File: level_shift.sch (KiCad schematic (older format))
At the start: 3 parts, among them Q1 BSS138

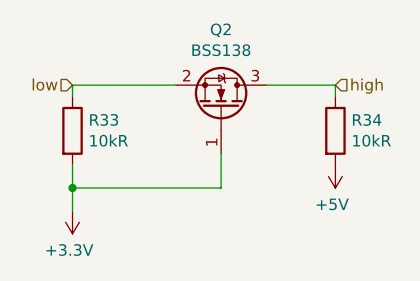
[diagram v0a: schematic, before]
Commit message: with cms resistors
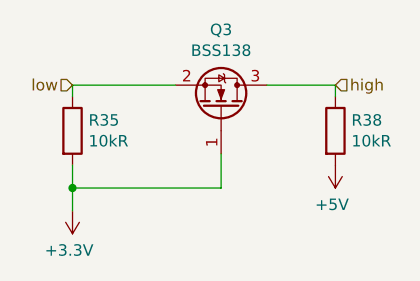
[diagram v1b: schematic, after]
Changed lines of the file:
@@
 AR Path="/619197DB/61901F6C" Ref="Q2"  Part="1"
 AR Path="/6191A86C/61901F6C" Ref="Q3"  Part="1"
-F 0 "Q2" V 4192 2200 50  0000 C CNN
+F 0 "Q3" V 4192 2200 50  0000 C CNN
 F 1 "BSS138" V 4101 2200 50  0000 C CNN
 F 2 "Package_TO_SOT_SMD:SOT-23" H 4050 2125 50  0001 L CIN
@@
 AR Path="/619197DB/61905F85" Ref="R33"  Part="1"
 AR Path="/6191A86C/61905F85" Ref="R35"  Part="1"
-F 0 "R33" H 3270 2346 50  0000 L CNN
+F 0 "R35" H 3270 2346 50  0000 L CNN
 F 1 "10kR" H 3270 2255 50  0000 L CNN
 F 2 "Resistor_SMD:R_0805_2012Metric_Pad1.20x1.40mm_HandSolder" V 3130 2300 50  0001 C CNN
@@
 AR Path="/619197DB/619062D3" Ref="R34"  Part="1"
 AR Path="/6191A86C/619062D3" Ref="R38"  Part="1"
-F 0 "R34" H 4420 2346 50  0000 L CNN
+F 0 "R38" H 4420 2346 50  0000 L CNN
 F 1 "10kR" H 4420 2255 50  0000 L CNN
 F 2 "Resistor_SMD:R_0805_2012Metric_Pad1.20x1.40mm_HandSolder" V 4280 2300 50  0001 C CNN
@@
 AR Path="/619197DB/619071C9" Ref="#PWR0105"  Part="1"
 AR Path="/6191A86C/619071C9" Ref="#PWR0137"  Part="1"
-F 0 "#PWR0105" H 3200 2500 50  0001 C CNN
+F 0 "#PWR0137" H 3200 2500 50  0001 C CNN
 F 1 "+3.3V" H 3215 2823 50  0000 C CNN
 F 2 "" H 3200 2650 50  0001 C CNN
@@
 AR Path="/619197DB/619081A9" Ref="#PWR0136"  Part="1"
 AR Path="/6191A86C/619081A9" Ref="#PWR0138"  Part="1"
-F 0 "#PWR0136" H 4350 2300 50  0001 C CNN
+F 0 "#PWR0138" H 4350 2300 50  0001 C CNN
 F 1 "+5V" H 4365 2623 50  0000 C CNN
 F 2 "" H 4350 2450 50  0001 C CNN
